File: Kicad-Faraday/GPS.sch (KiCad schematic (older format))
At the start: 5 parts, among them U7 M10478-A2

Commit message: Adding Rev D files for night
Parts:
- gave numbers to parts that had none: 1
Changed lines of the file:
@@
 Sheet 9 11
 Title "Faraday Wireless Node"
-Date "13 nov 2016"
+Date "14 nov 2016"
 Rev "C"
 Comp "FaradayRF"
@@
 	4400 5050 7300 5050
 $Comp
-L C C?
+L C C15
 U 1 1 582878DD
 P 6800 4550
-F 0 "C?" V 6850 4600 50  0000 L CNN
+F 0 "C15" V 6850 4600 50  0000 L CNN
 F 1 "12pF" V 6850 4300 50  0000 L CNN
 F 2 "C0402" V 6750 4750 50  0000 C CNN

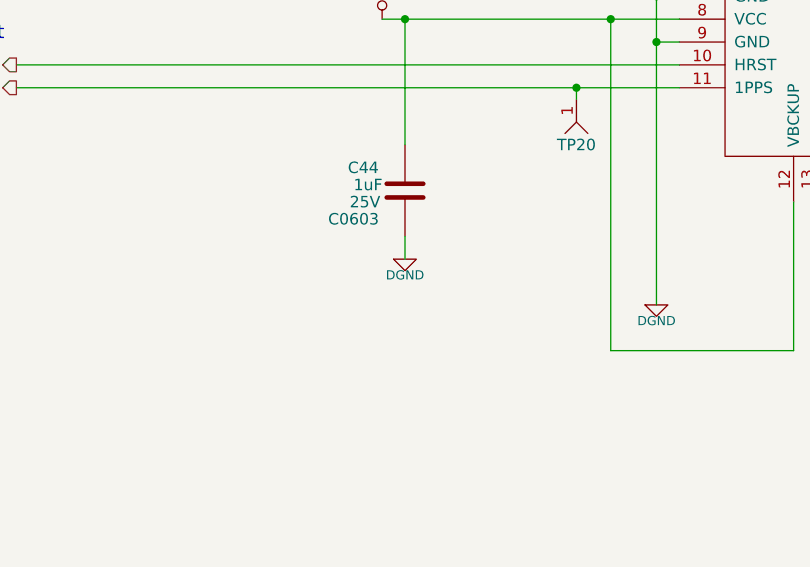
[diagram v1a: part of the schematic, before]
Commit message: Cleaned up a few connections on the schematic to make sure wire junctions were used. Also added a few notes such as LED color. Output new PDF of Schematics and updated Rev to Rev D1 for PCB:NG
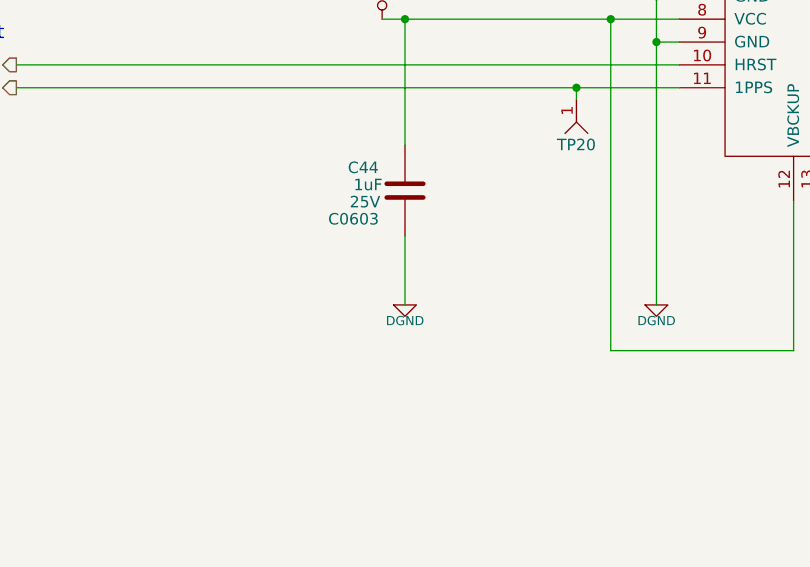
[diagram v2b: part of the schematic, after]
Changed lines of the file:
@@
 Sheet 9 11
 Title "Faraday Wireless Node"
-Date "14 nov 2016"
-Rev "C"
+Date "15 nov 2016"
+Rev "D1"
 Comp "FaradayRF"
 Comment1 "www.FaradayRF.com"
@@
 L DGND #PWR090
 U 1 1 55C1E57A
-P 6100 5800
-F 0 "#PWR090" H 6100 5800 40  0001 C CNN
-F 1 "DGND" H 6100 5730 40  0000 C CNN
-F 2 "~" H 6100 5800 60  0000 C CNN
-F 3 "~" H 6100 5800 60  0000 C CNN
-	1    6100 5800
+P 6100 6000
+F 0 "#PWR090" H 6100 6000 40  0001 C CNN
+F 1 "DGND" H 6100 5930 40  0000 C CNN
+F 2 "~" H 6100 6000 60  0000 C CNN
+F 3 "~" H 6100 6000 60  0000 C CNN
+	1    6100 6000
 	1    0    0    -1
 $EndComp
@@
 	8300 5650 8300 5550
 Wire Wire Line
-	6100 5800 6100 5700
+	6100 6000 6100 5700
 Wire Wire Line
 	6000 4750 7300 4750
